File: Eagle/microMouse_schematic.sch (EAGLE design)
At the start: 35 parts, among them IC1 DSPIC33FJ64MC804-PT, IC2 L293D, X1 332-06, X2 332-06, X3 057-006-1, X4 057-006-1, X6 22-23-2021

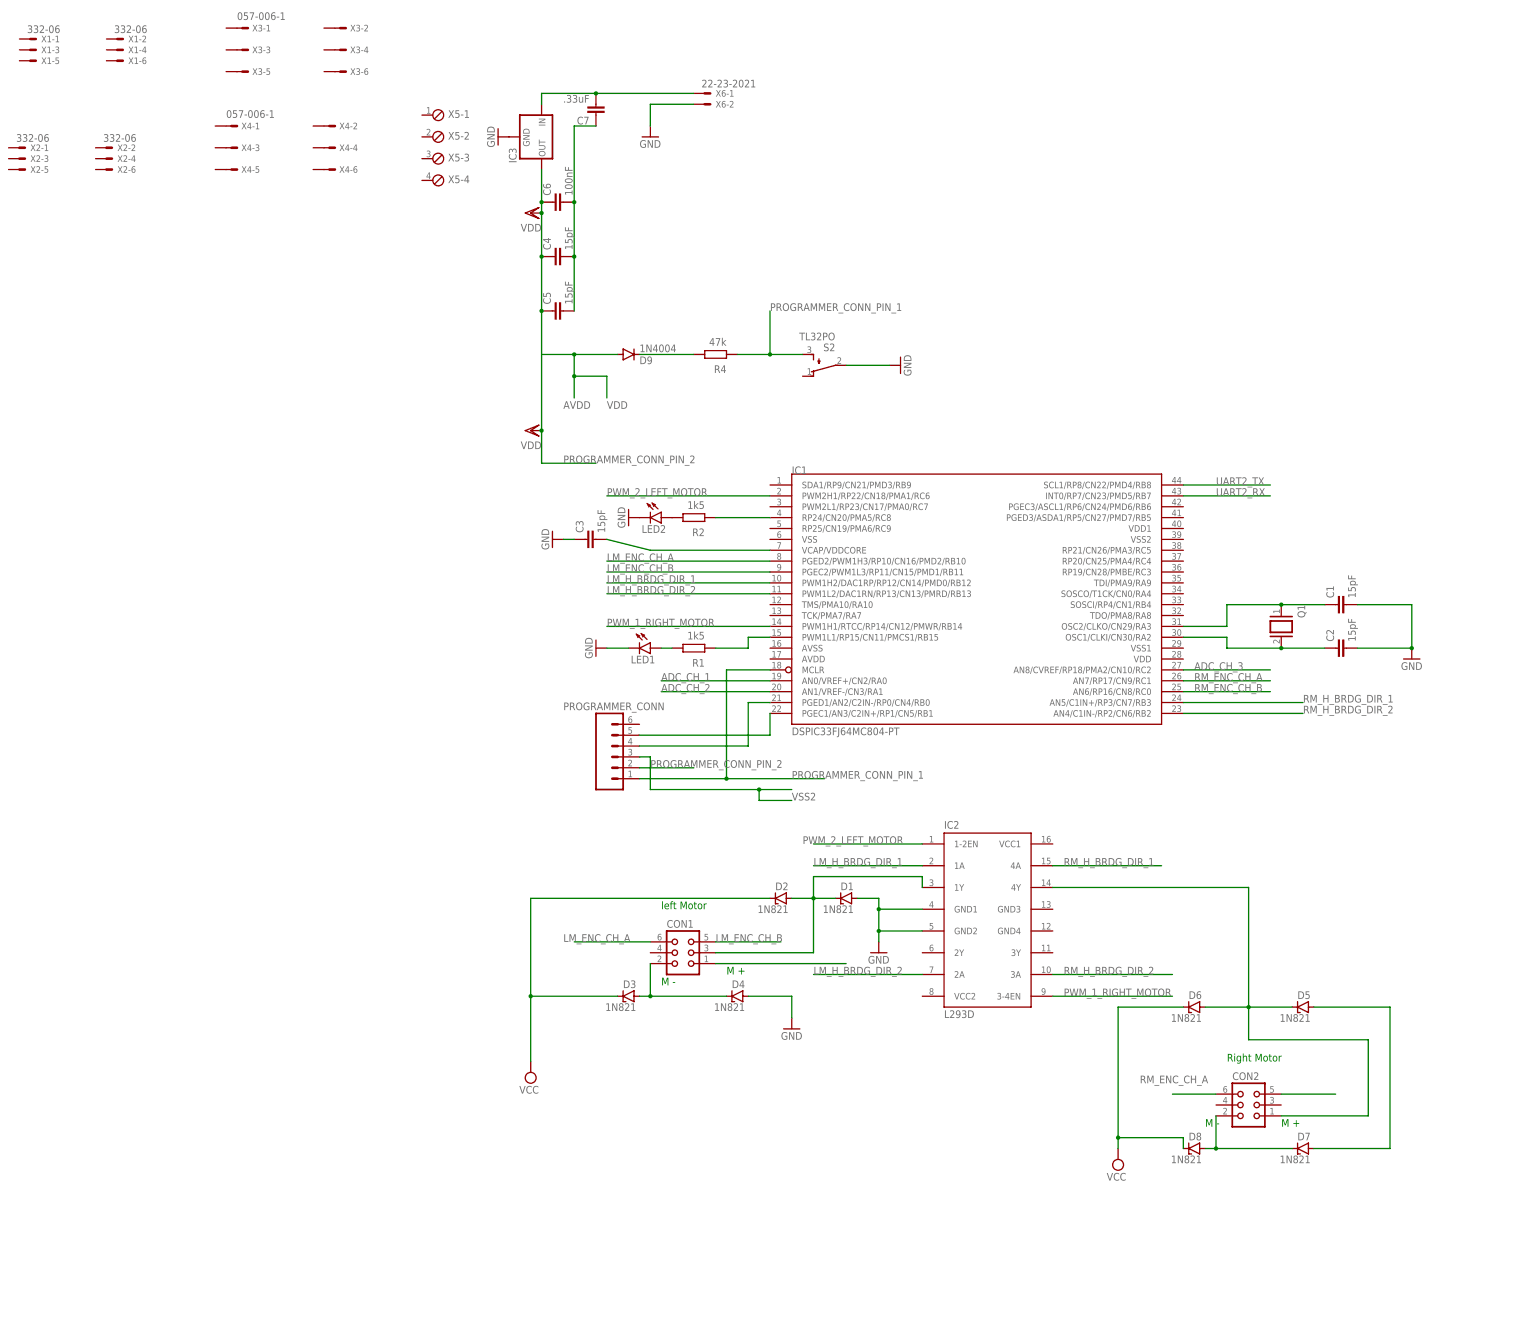
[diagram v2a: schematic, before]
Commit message: finish PID [untested] , finish schematic
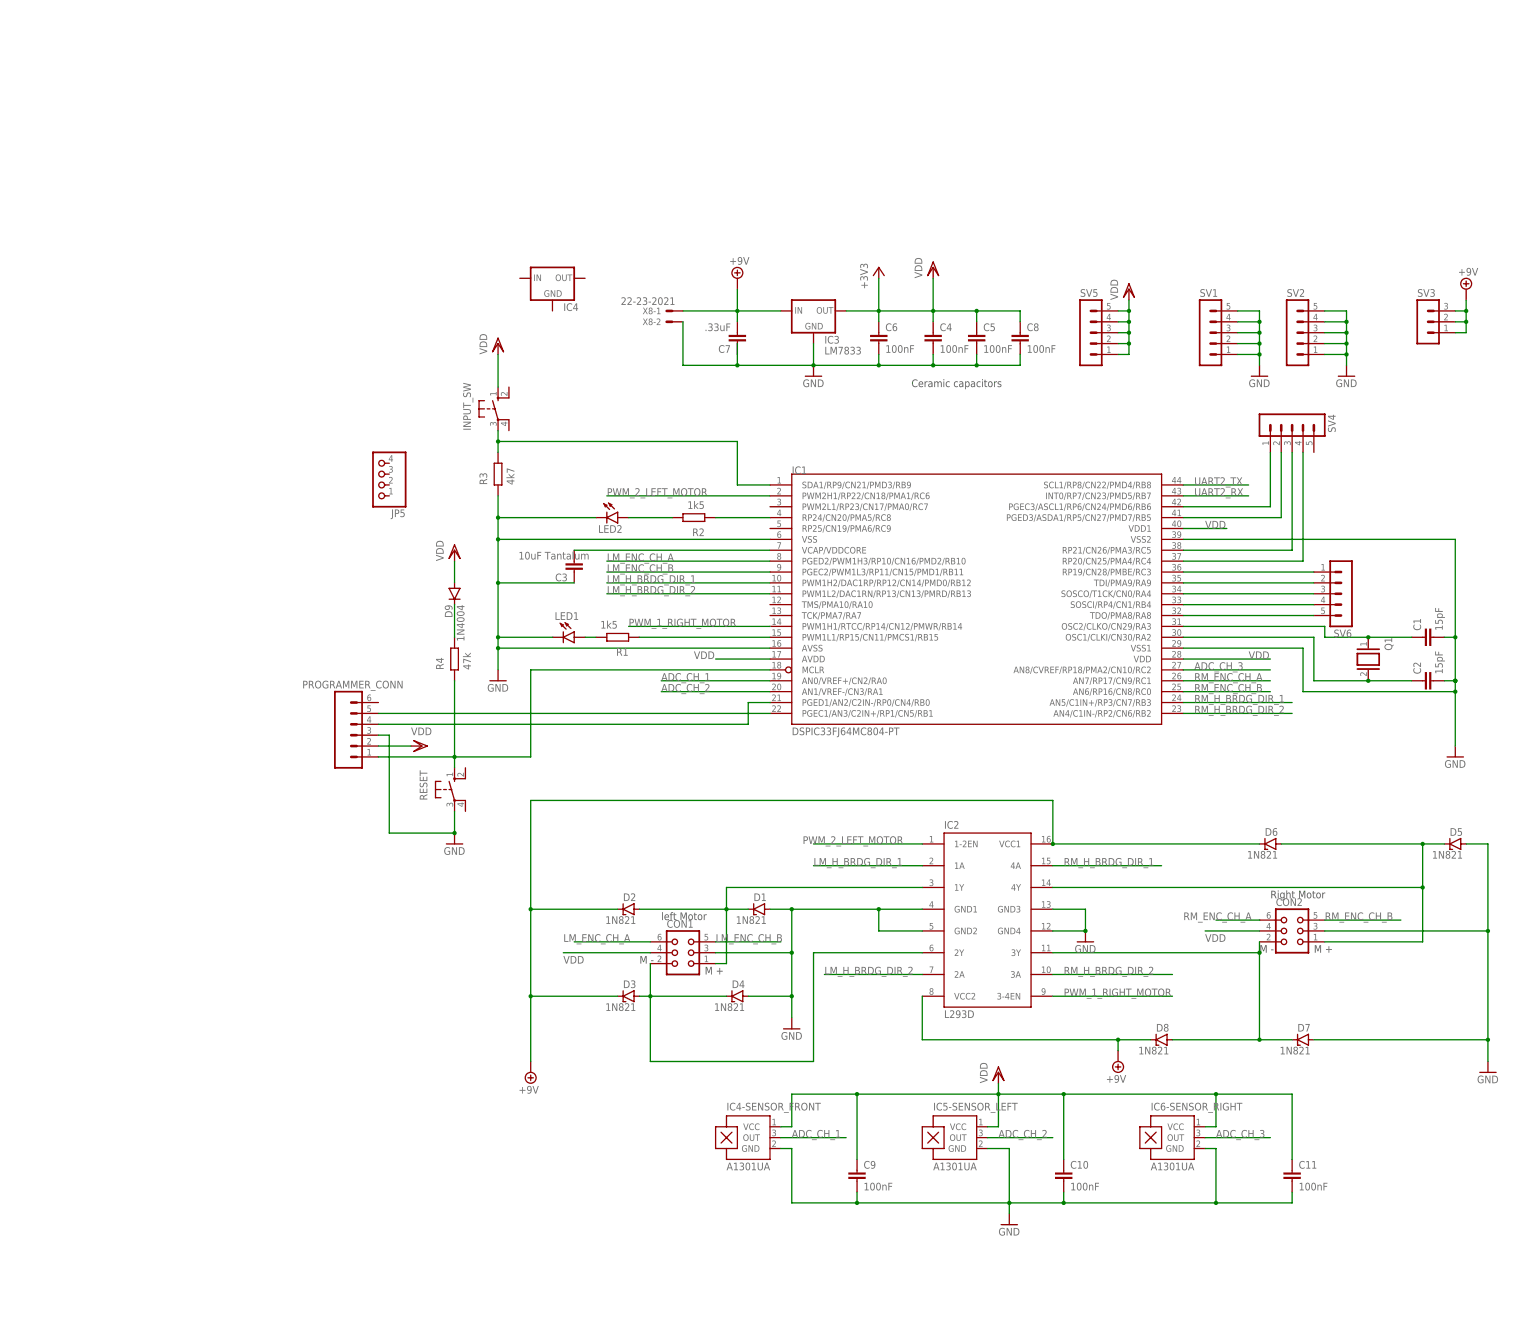
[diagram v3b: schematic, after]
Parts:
- removed S2: TL32PO, switch:TL32PO
- removed X1, X2: 332-06, con-garry:332-06
- removed X3, X4: 057-006-1, con-panduit:057-006-1
- removed X5: (no value), con-phoenix-254:MPT4
- removed X6: 22-23-2021, con-molex:22-23-2021
- added C10, C11, C8, C9: 100nF, capacitor-wima:C2,5-3
- added IC4: (no value), v-reg:78XXS
- added IC4-SENSOR_FRONT, IC5-SENSOR_LEFT, IC6-SENSOR_RIGHT: A1301UA, allegro:A1301UA
- added INPUT_SW, RESET: (no value), switch-omron:10-XX
- added JP5: (no value), pinhead:PINHD-1X4
- added R3: 4k7, ngspice-simulation:R
- added SV1, SV2, SV4, SV5, SV6: (no value), con-lstb:MA05-1
- added SV3: (no value), con-lstb:MA03-1
- added X8: 22-23-2021, con-molex:22-23-2021
- C3: value 15pF -> 10uF Tantalum
- C4, C5: value 15pF -> 100nF
- IC3: value (none) -> LM7833; device v-reg:78LXX -> v-reg:78XXS
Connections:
- removed net AVDD: D9.A
- removed net N$2 (its old number): CON2.5
- removed net PROGRAMMER_CONN_PIN_1: IC1.MCLR, PROGRAMMER_CONN.1, R4.1, S2.S
- removed net PROGRAMMER_CONN_PIN_2: C4.1, C5.1, C6.1, IC3.OUT, PROGRAMMER_CONN.2
- removed net VCC: D2.C, D3.C, D6.C, D8.C
- removed net VSS2: PROGRAMMER_CONN.3
- new net +9V: C7.2, D2.C, D3.C, D6.C, D8.C, IC2.VCC1, IC2.VCC2, IC3.IN, SV3.1, SV3.2, SV3.3, X8-1.S
- new net N$15: IC1.SOSCI/RP4/CN1/RB4, SV6.4
- new net N$18: IC1.TDI/PMA9/RA9, SV6.2
- new net N$20: IC1.RP19/CN28/PMBE/RC3, SV6.1
- new net N$23: IC1.PGED3/ASDA1/RP5/CN27/PMD7/RB5, SV4.2
- new net N$24: IC1.RP21/CN26/PMA3/RC5, SV4.3
- new net N$8: IC1.SDA1/RP9/CN21/PMD3/RB9, INPUT_SW.P, R3.2
- new net RESET: IC1.MCLR, PROGRAMMER_CONN.1, R4.1, RESET.S
- new net VDD: C10.1, C11.1, C4.1, C5.1, C6.1, C8.1, C9.1, CON1.4, CON2.4, D9.A, IC1.AVDD, IC1.VDD, IC1.VDD1, IC3.OUT, IC4-SENSOR_FRONT.VCC, IC5-SENSOR_LEFT.VCC, IC6-SENSOR_RIGHT.VCC, INPUT_SW.S, PROGRAMMER_CONN.2, SV5.1, SV5.2, SV5.3, SV5.4, SV5.5
- net ADC_CH_1: now also IC4-SENSOR_FRONT.OUT
- net ADC_CH_2: now also IC5-SENSOR_LEFT.OUT
- net ADC_CH_3: now also IC6-SENSOR_RIGHT.OUT
- net GND: now also C10.2, C11.2, C4.2, C5.2, C6.2, C7.1, C8.2, C9.2, CON1.3, CON2.3, D5.A, D7.A, IC1.AVSS, IC1.VSS, IC1.VSS1, IC1.VSS2, IC2.GND3, IC2.GND4, IC4-SENSOR_FRONT.GND, IC5-SENSOR_LEFT.GND, IC6-SENSOR_RIGHT.GND, PROGRAMMER_CONN.3, R3.1, RESET.P, SV1.1, SV1.2, SV1.3, SV1.4, SV1.5, SV2.1, SV2.2, SV2.3, SV2.4, SV2.5, X8-2.S; no longer S2.P, X6-2.S
- net N$16: now also IC1.SOSCO/T1CK/CN0/RA4, SV6.3; no longer CON2.2, D7.C, D8.A
- net N$21: now also IC1.RP20/CN25/PMA4/RC4, SV4.4; no longer C4.2, C5.2, C6.2, C7.1
- net N$22: now also IC1.PGEC3/ASCL1/RP6/CN24/PMD6/RB6, SV4.1; no longer C7.2, IC3.IN, X6-1.S
- net N$4: now also CON1.1; no longer CON1.3
- net N$6: now also CON2.2, D7.C, D8.A, IC2.3Y; no longer CON1.1
- net N$7: now also IC2.2Y
- net N$9: now also IC1.TDO/PMA8/RA8, SV6.5; no longer D5.A, D7.A
- net RM_ENC_CH_B: now also CON2.5
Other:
- note added: "Ceramic capacitors"
- note removed: "AVDD"
- note removed: "VDD"
- moved on the sheet: C1, C2, C3, C4, C5, C6, C7, CON2, D1, D2, D5, D6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

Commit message: add UART socket to schematic, adjust Voltage reg
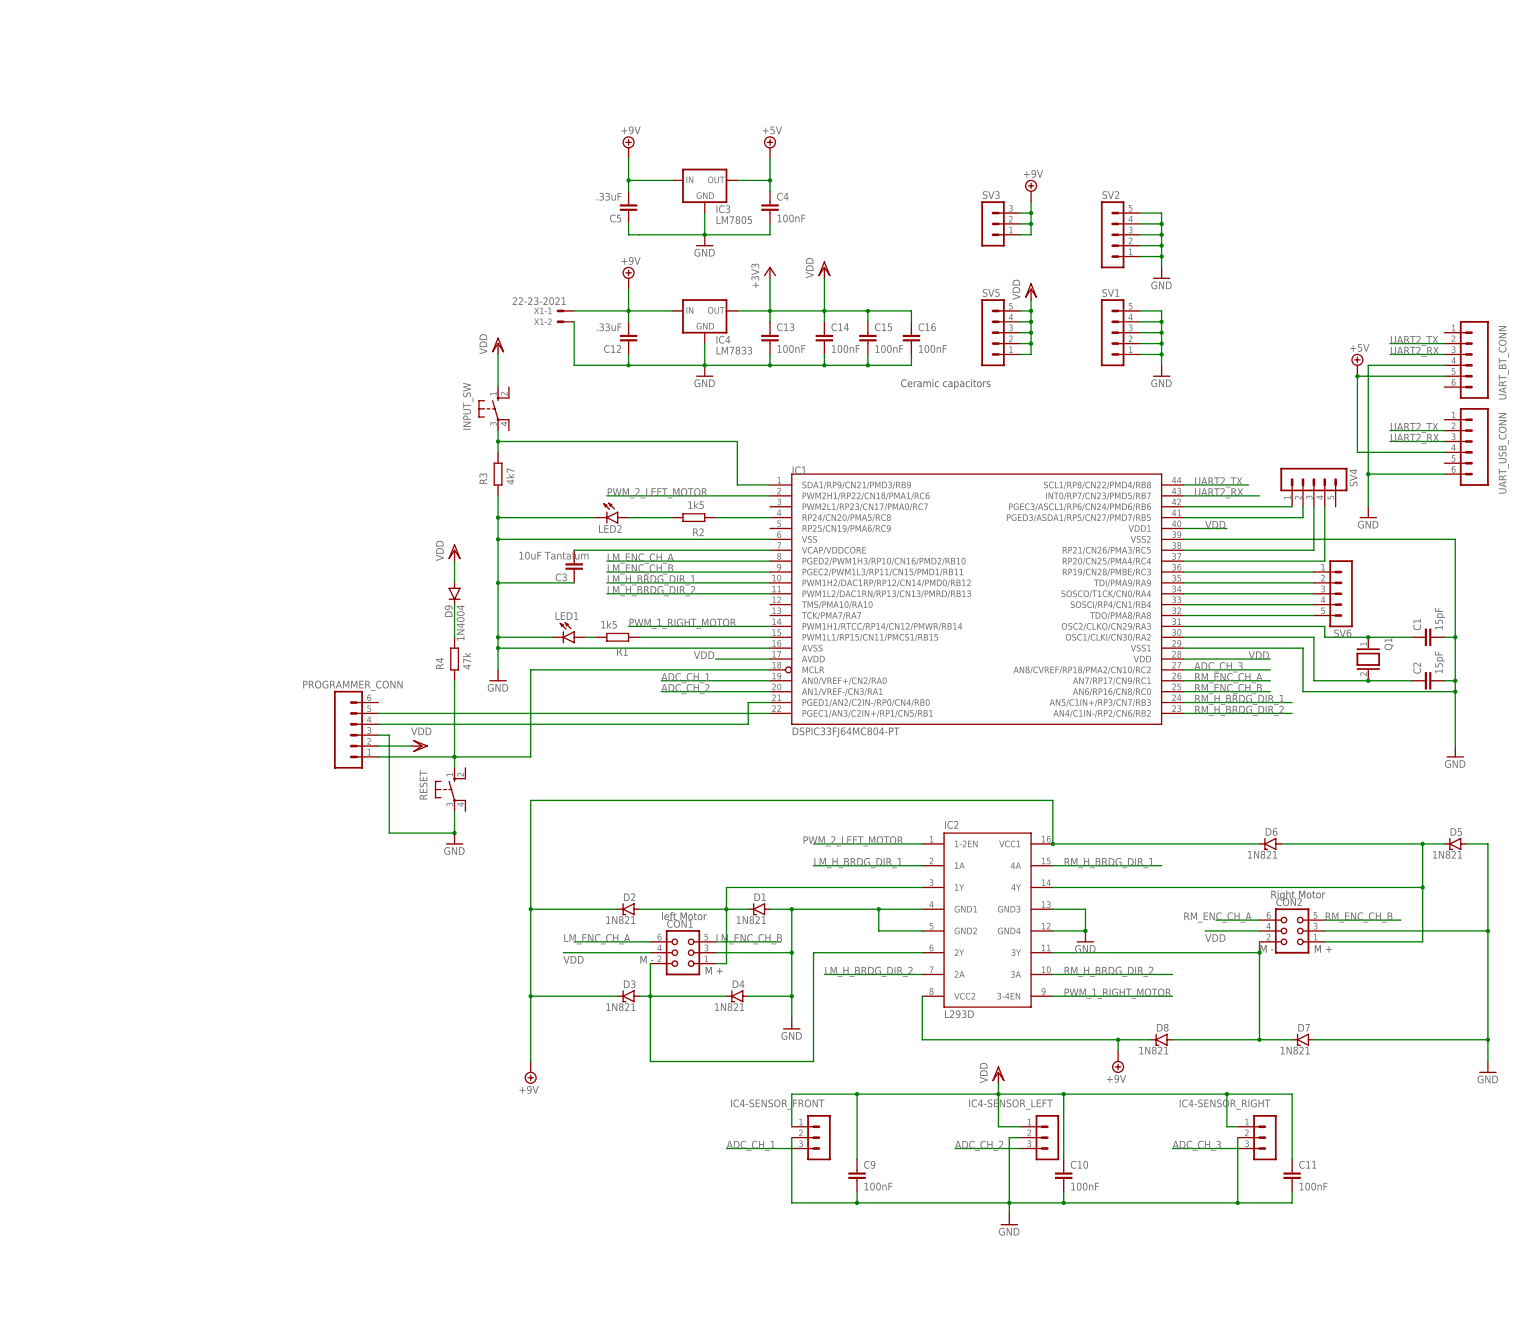
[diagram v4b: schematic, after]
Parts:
- removed C6, C8: 100nF, capacitor-wima:C2,5-3
- removed C7: .33uF, capacitor-wima:C2,5-3
- removed IC5-SENSOR_LEFT, IC6-SENSOR_RIGHT: A1301UA, allegro:A1301UA
- removed JP5: (no value), pinhead:PINHD-1X4
- removed X8: 22-23-2021, con-molex:22-23-2021
- added C12: .33uF, capacitor-wima:C2,5-3
- added C13, C14, C15, C16: 100nF, capacitor-wima:C2,5-3
- added IC4-SENSOR_LEFT, IC4-SENSOR_RIGHT: (no value), con-lstb:MA03-1
- added UART_BT_CONN, UART_USB_CONN: (no value), con-amp-quick:M06
- added X1: 22-23-2021, con-molex:22-23-2021
- C5: value 100nF -> .33uF
- IC3: value LM7833 -> LM7805
- IC4: value (none) -> LM7833
- IC4-SENSOR_FRONT: value A1301UA -> (none); device allegro:A1301UA -> con-lstb:MA03-1
- LED1, LED2: device led:LED -> led:LED5MM
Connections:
- new net +5V: C4.1, IC3.OUT, UART_BT_CONN.5, UART_USB_CONN.4
- net +9V: now also C12.2, C5.2, IC4.IN, X1-1.S; no longer C7.2, X8-1.S
- net ADC_CH_1: now also IC4-SENSOR_FRONT.3; no longer IC4-SENSOR_FRONT.OUT
- net ADC_CH_2: now also IC4-SENSOR_LEFT.3; no longer IC5-SENSOR_LEFT.OUT
- net ADC_CH_3: now also IC4-SENSOR_RIGHT.3; no longer IC6-SENSOR_RIGHT.OUT
- net GND: now also C12.1, C13.2, C14.2, C15.2, C16.2, C5.1, IC4-SENSOR_FRONT.2, IC4-SENSOR_LEFT.2, IC4-SENSOR_RIGHT.2, IC4.GND, UART_BT_CONN.4, UART_USB_CONN.6, X1-2.S; no longer C5.2, C6.2, C7.1, C8.2, IC4-SENSOR_FRONT.GND, IC5-SENSOR_LEFT.GND, IC6-SENSOR_RIGHT.GND, X8-2.S
- net UART2_RX: now also UART_BT_CONN.3, UART_USB_CONN.3
- net UART2_TX: now also UART_BT_CONN.2, UART_USB_CONN.2
- net VDD: now also C13.1, C14.1, C15.1, C16.1, IC4-SENSOR_FRONT.1, IC4-SENSOR_LEFT.1, IC4-SENSOR_RIGHT.1, IC4.OUT; no longer C4.1, C5.1, C6.1, C8.1, IC3.OUT, IC4-SENSOR_FRONT.VCC, IC5-SENSOR_LEFT.VCC, IC6-SENSOR_RIGHT.VCC
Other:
- moved on the sheet: C4, C5, IC3, IC4, SV1, SV2, SV3, SV4, SV5
